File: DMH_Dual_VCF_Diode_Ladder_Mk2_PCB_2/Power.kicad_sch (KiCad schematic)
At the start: 38 parts, among them J0 Conn_01x01, J100 IDC_02x08, J23 Conn_01x04_PinHeader, U1 TL074, U10 TL074, U2 TL074, U3 TL074, U4 TL074, U5 TL074, U6 TL074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

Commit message: Complete Exclude From Board on PCB 2
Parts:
- J23: footprint Connector_PinHeader_2.54mm:PinHeader_1x04_P2.54mm_Vertical -> Connector_PinSocket_2.54mm:PinSocket_1x04_P2.54mm_Vertical
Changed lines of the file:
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@@
 		(exclude_from_sim no)
 		(in_bom yes)
-		(on_board yes)
+		(on_board no)
 		(dnp no)
 		(fields_autoplaced yes)
@@
 			)
 		)
-		(property "Footprint" "Connector_PinHeader_2.54mm:PinHeader_1x04_P2.54mm_Vertical"
+		(property "Footprint" "Connector_PinSocket_2.54mm:PinSocket_1x04_P2.54mm_Vertical"
 			(at 88.9 57.15 0)
 			(effects
@@
 			)
 		)
-		(property "Footprint" "Connector_PinHeader_2.54mm:PinHeader_1x04_P2.54mm_Vertical"
+		(property "Footprint" "Connector_PinSocket_2.54mm:PinSocket_1x04_P2.54mm_Vertical"
 			(at 88.9 69.85 0)
 			(effects
@@
 			)
 		)
-		(property "Footprint" "Connector_PinHeader_2.54mm:PinHeader_1x04_P2.54mm_Vertical"
+		(property "Footprint" "Connector_PinSocket_2.54mm:PinSocket_1x04_P2.54mm_Vertical"
 			(at 88.9 50.8 0)
 			(effects
@@
 			)
 		)
-		(property "Footprint" "Connector_PinHeader_2.54mm:PinHeader_1x04_P2.54mm_Vertical"
+		(property "Footprint" "Connector_PinSocket_2.54mm:PinSocket_1x04_P2.54mm_Vertical"
 			(at 88.9 63.5 0)
 			(effects
@@
 		(exclude_from_sim no)
 		(in_bom yes)
-		(on_board yes)
+		(on_board no)
 		(dnp no)
 		(fields_autoplaced yes)

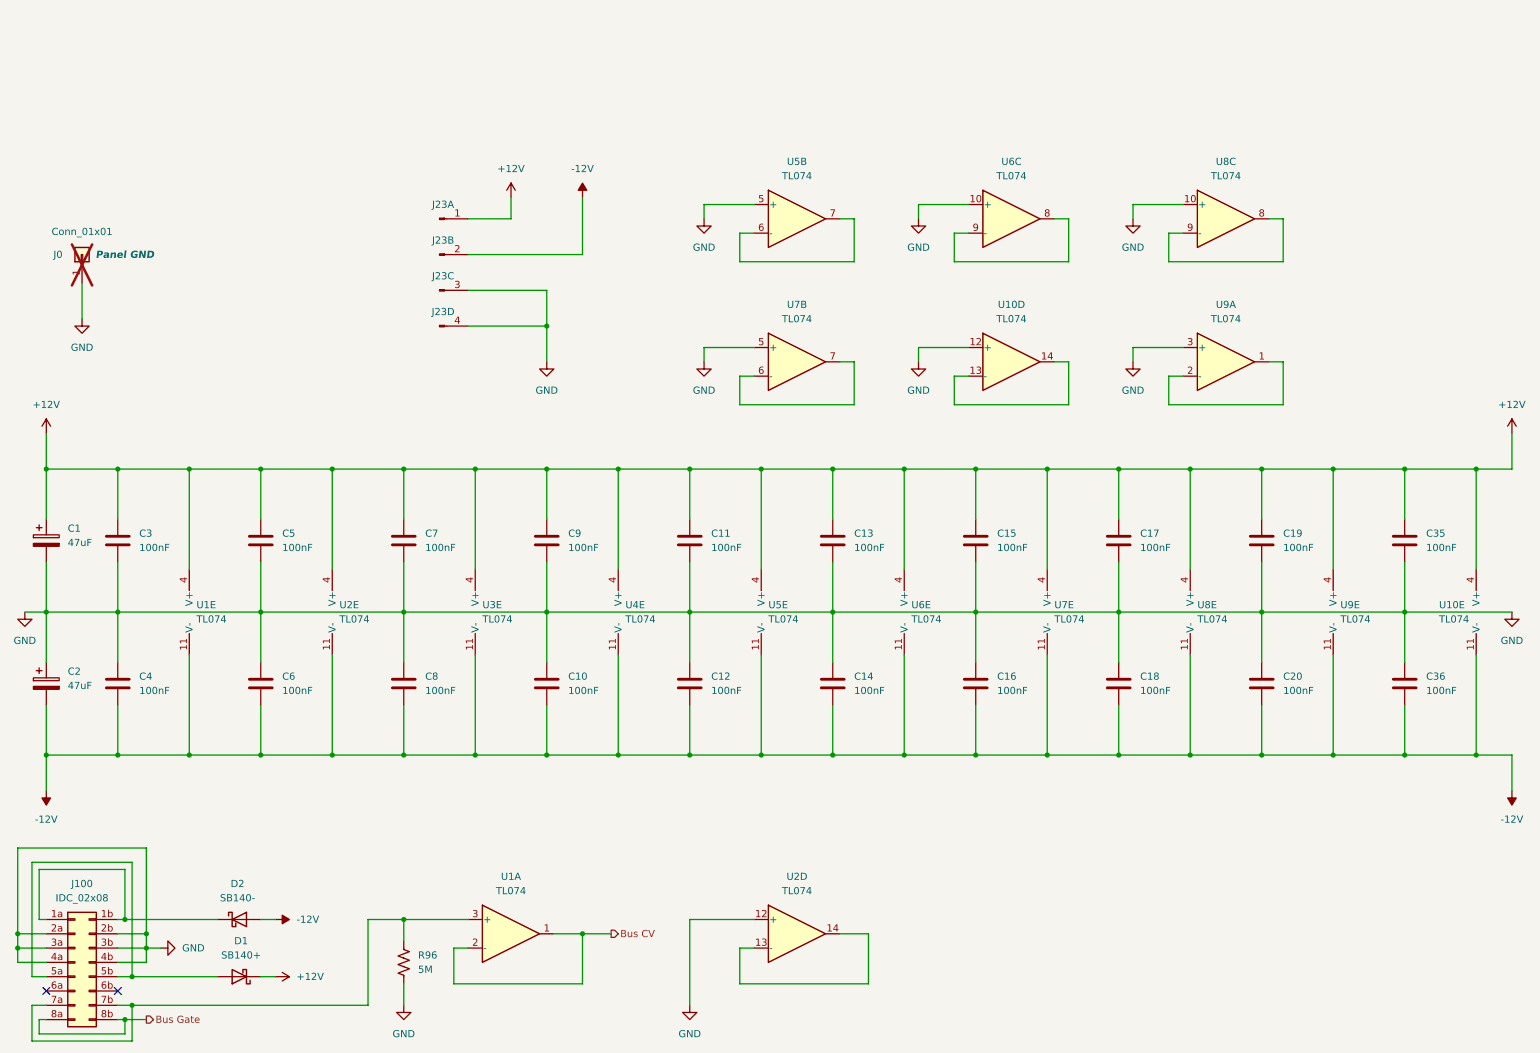
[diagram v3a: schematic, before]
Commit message: Added buffering to each CV 3 input separately
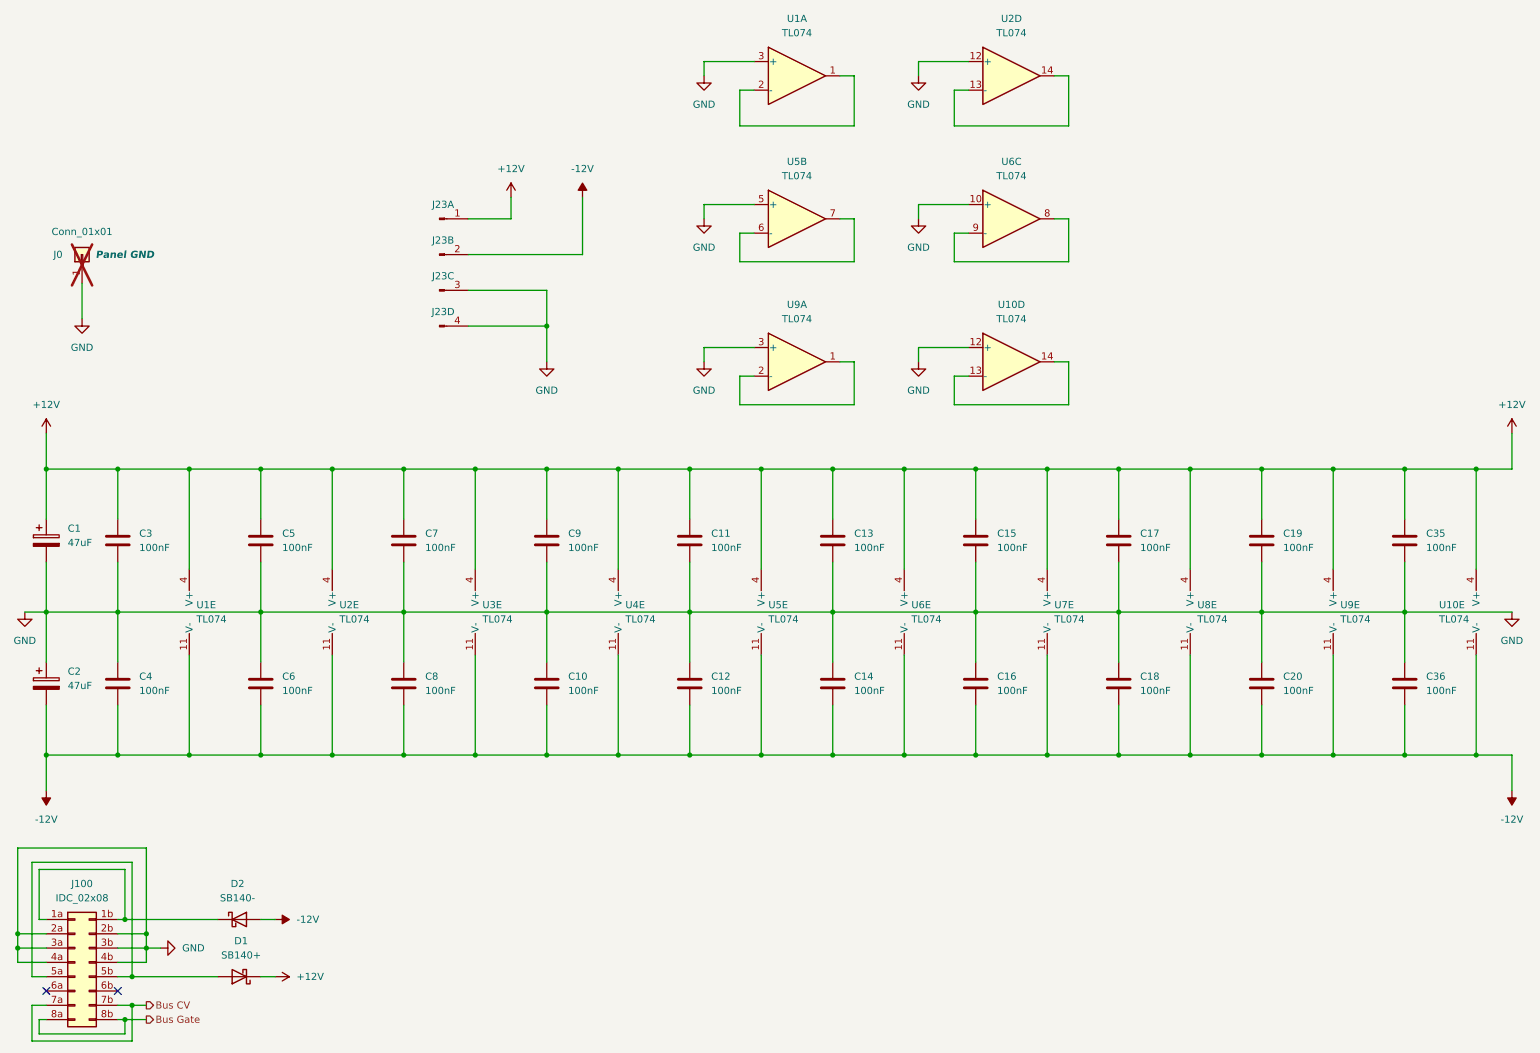
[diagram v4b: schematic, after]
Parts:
- removed R96: 5M, Resistor_THT:R_Axial_DIN0207_L6.3mm_D2.5mm_P7.62mm_Horizontal, symbol Device:R_US
- removed unit 2 of U7
- removed unit 3 of U8
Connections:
- net Bus CV: now also J100.7a (Pin_7a), J100.7b (Pin_7b); no longer U1.1, U1.2 (-)
- net GND: now also U1.3 (+)
- new net: U1.1, U1.2 (-)
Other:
- moved on the sheet: U1A, U2D, U9A

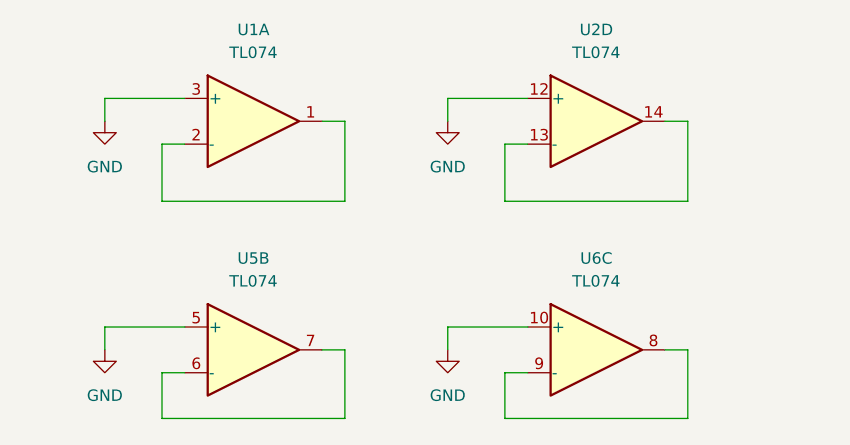
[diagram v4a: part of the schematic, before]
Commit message: Synchronized changes from PCB 1 to PCB 2 schematic
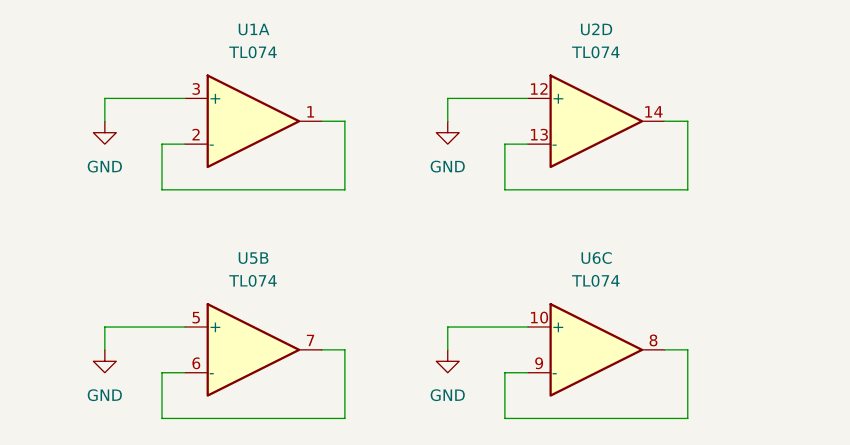
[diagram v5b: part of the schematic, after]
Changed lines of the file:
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@@
 	(wire
 		(pts
-			(xy 162.56 34.29) (xy 162.56 25.4)
+			(xy 162.56 33.02) (xy 162.56 25.4)
 		)
 		(stroke
@@
 	(wire
 		(pts
-			(xy 142.24 34.29) (xy 162.56 34.29)
+			(xy 142.24 33.02) (xy 162.56 33.02)
 		)
 		(stroke
@@
 	(wire
 		(pts
-			(xy 200.66 25.4) (xy 200.66 34.29)
+			(xy 200.66 25.4) (xy 200.66 33.02)
 		)
 		(stroke
@@
 	(wire
 		(pts
-			(xy 200.66 34.29) (xy 180.34 34.29)
+			(xy 200.66 33.02) (xy 180.34 33.02)
 		)
 		(stroke
@@
 	(wire
 		(pts
-			(xy 142.24 27.94) (xy 142.24 34.29)
+			(xy 142.24 27.94) (xy 142.24 33.02)
 		)
 		(stroke
@@
 	(wire
 		(pts
-			(xy 180.34 34.29) (xy 180.34 27.94)
-		)
-		(stroke
+			(xy 180.34 33.02) (xy 180.34 27.94)
+		)
+		(stroke

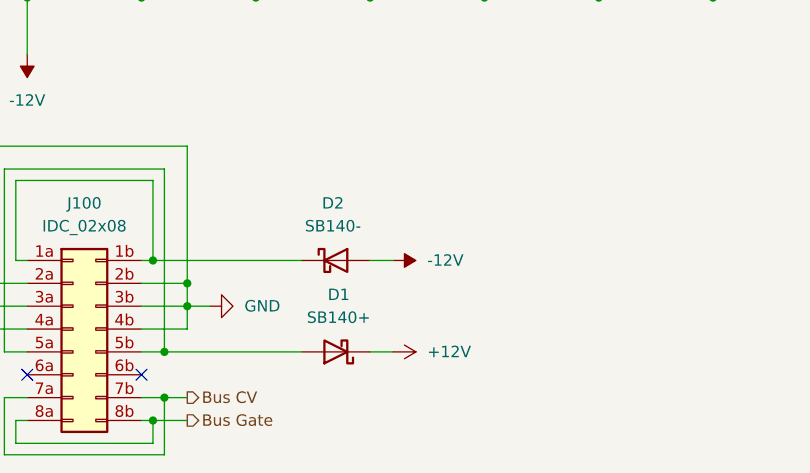
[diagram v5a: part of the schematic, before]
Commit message: KiCad 9.0.7 + centralized library
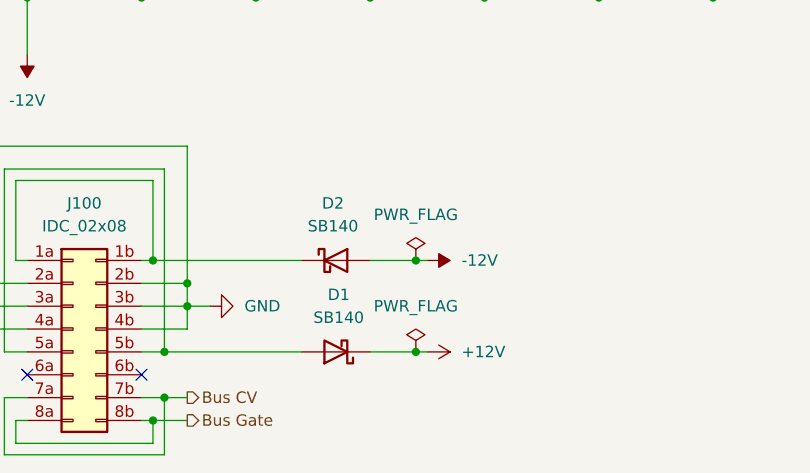
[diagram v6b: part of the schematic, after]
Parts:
- D1: value SB140+ -> SB140; symbol SynthStuff:Power_Bus_Schotty_+ -> Diode:SB140
- D2: value SB140- -> SB140; symbol SynthStuff:Power_Bus_Schotty_- -> Diode:SB140
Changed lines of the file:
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@@
 	)
 	(junction
+		(at 62.23 175.26)
+		(diameter 0)
+		(color 0 0 0 0)
+	)
+	(junction
 		(at 31.75 95.25)
 		(diameter 0)
@@
 	)
 	(junction
+		(at 62.23 185.42)
+		(diameter 0)
+		(color 0 0 0 0)
+	)
+	(junction
 		(at 36.83 177.8)
 		(diameter 0)
@@
 	(wire
 		(pts
-			(xy 57.15 175.26) (xy 59.69 175.26)
+			(xy 57.15 175.26) (xy 62.23 175.26)
 		)
 		(stroke
@@
 	(wire
 		(pts
-			(xy 57.15 185.42) (xy 59.69 185.42)
+			(xy 57.15 185.42) (xy 62.23 185.42)
 		)
 		(stroke
@@
 	(wire
 		(pts
+			(xy 62.23 185.42) (xy 63.5 185.42)
+		)
+		(stroke
+			(width 0)
+			(type default)
+		)
+	)
+	(wire
+		(pts
 			(xy 133.35 146.05) (xy 146.05 146.05)
 		)
@@
 	(wire
 		(pts
+			(xy 62.23 175.26) (xy 63.5 175.26)
+		)
+		(stroke
+			(width 0)
+			(type default)
+		)
+	)
+	(wire
+		(pts
 			(xy 135.89 50.8) (xy 135.89 48.26)
 		)
@@
 	(symbol
 		(lib_id "power:+12V")
-		(at 59.69 185.42 270)
+		(at 63.5 185.42 270)
 		(unit 1)
 		(exclude_from_sim no)
@@
 		(fields_autoplaced yes)
 		(property "Reference" "#PWR02"
-			(at 55.88 185.42 0)
+			(at 59.69 185.42 0)
 			(effects
 				(font
@@
 		)
 		(property "Value" "+12V"
-			(at 63.5 185.4199 90)
+			(at 67.31 185.4199 90)
 			(effects
 				(font
@@
 		)
 		(property "Footprint" ""
-			(at 59.69 185.42 0)
+			(at 63.5 185.42 0)
 			(effects
 				(font
@@
 		)
 		(property "Datasheet" ""
-			(at 59.69 185.42 0)
+			(at 63.5 185.42 0)
 			(effects
 				(font
@@
 		)
 		(property "Description" "Power symbol creates a global label with name \"+12V\""
-			(at 59.69 185.42 0)
+			(at 63.5 185.42 0)
 			(effects
 				(font
@@
 	)
 	(symbol
+		(lib_id "power:PWR_FLAG")
+		(at 62.23 185.42 0)
+		(unit 1)
+		(exclude_from_sim no)
+		(in_bom yes)
+		(on_board yes)
+		(dnp no)
+		(fields_autoplaced yes)
+		(property "Reference" "#FLG02"
+			(at 62.23 183.515 0)
+			(effects
+				(font
+					(size 1.27 1.27)
+				)
+				(hide yes)
+			)
+		)
+		(property "Value" "PWR_FLAG"
+			(at 62.23 180.34 0)
+			(effects
+				(font
+					(size 1.27 1.27)
+				)
+			)
+		)
+		(property "Footprint" ""
+			(at 62.23 185.42 0)
+			(effects
+				(font
+					(size 1.27 1.27)
+				)
+				(hide yes)
+			)
+		)
+		(property "Datasheet" "~"
+			(at 62.23 185.42 0)
+			(effects
+				(font
+					(size 1.27 1.27)
+				)
+				(hide yes)
+			)
+		)
+		(property "Description" "Special symbol for telling ERC where power comes from"
+			(at 62.23 185.42 0)
+			(effects
+				(font
+					(size 1.27 1.27)
+				)
+				(hide yes)
+			)
+		)
+		(pin "1"
+		)
+		(instances
+			(project ""
+				(path "/58f4306d-5387-4983-bb08-41a2313fd315/0cdf34b2-39cd-4d9e-981a-97cd34791509"
+					(reference "#FLG02")
+					(unit 1)
+				)
+			)
+		)
+	)
+	(symbol
 		(lib_id "power:GND")
 		(at 135.89 50.8 0)
@@
 	)
 	(symbol
+		(lib_id "power:PWR_FLAG")
+		(at 62.23 175.26 0)
+		(unit 1)
+		(exclude_from_sim no)
+		(in_bom yes)
+		(on_board yes)
+		(dnp no)
+		(fields_autoplaced yes)
+		(property "Reference" "#FLG01"
+			(at 62.23 173.355 0)
+			(effects
+				(font
+					(size 1.27 1.27)
+				)
+				(hide yes)
+			)
+		)
+		(property "Value" "PWR_FLAG"
+			(at 62.23 170.18 0)
+			(effects
+				(font
+					(size 1.27 1.27)
+				)
+			)
+		)
+		(property "Footprint" ""
+			(at 62.23 175.26 0)
+			(effects
+				(font
+					(size 1.27 1.27)
+				)
+				(hide yes)
+			)
+		)
+		(property "Datasheet" "~"
+			(at 62.23 175.26 0)
+			(effects
+				(font
+					(size 1.27 1.27)
+				)
+				(hide yes)
+			)
+		)
+		(property "Description" "Special symbol for telling ERC where power comes from"
+			(at 62.23 175.26 0)
+			(effects
+				(font
+					(size 1.27 1.27)
+				)
+				(hide yes)
+			)
+		)
+		(pin "1"
+		)
+		(instances
+			(project ""
+				(path "/58f4306d-5387-4983-bb08-41a2313fd315/0cdf34b2-39cd-4d9e-981a-97cd34791509"
+					(reference "#FLG01")
+					(unit 1)
+				)
+			)
+		)
+	)
+	(symbol
 		(lib_id "Device:C")
 		(at 260.35 133.35 0)
@@
 	(symbol
 		(lib_id "power:-12V")
-		(at 59.69 175.26 270)
+		(at 63.5 175.26 270)
 		(unit 1)
 		(exclude_from_sim no)
@@
 		(fields_autoplaced yes)
 		(property "Reference" "#PWR01"
-			(at 55.88 175.26 0)
+			(at 59.69 175.26 0)
 			(effects
 				(font
@@
 		)
 		(property "Value" "-12V"
-			(at 63.5 175.2599 90)
+			(at 67.31 175.2599 90)
 			(effects
 				(font
@@
 		)
 		(property "Footprint" ""
-			(at 59.69 175.26 0)
+			(at 63.5 175.26 0)
 			(effects
 				(font
@@
 		)
 		(property "Datasheet" ""
-			(at 59.69 175.26 0)
+			(at 63.5 175.26 0)
 			(effects
 				(font
@@
 		)
 		(property "Description" "Power symbol creates a global label with name \"-12V\""
-			(at 59.69 175.26 0)
+			(at 63.5 175.26 0)
 			(effects
 				(font
@@
 	)
 	(symbol
-		(lib_id "SynthStuff:Power_Bus_Schotty_-")
+		(lib_id "Diode:SB140")
 		(at 53.34 175.26 0)
 		(unit 1)
@@
 			)
 		)
-		(property "Value" "SB140-"
+		(property "Value" "SB140"
 			(at 53.0225 171.45 0)
 			(effects
@@
 	)
 	(symbol
-		(lib_id "SynthStuff:Power_Bus_Schotty_+")
+		(lib_id "Diode:SB140")
 		(at 53.34 185.42 180)
 		(unit 1)
@@
 			)
 		)
-		(property "Value" "SB140+"
+		(property "Value" "SB140"
 			(at 53.6575 181.61 0)
 			(effects
